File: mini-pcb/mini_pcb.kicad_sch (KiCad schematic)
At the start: 34 parts, among them J1 IN, J2 OUT, J3 Barrel_Jack_Switch, J4 AUDIO_IN_TRS, J5 AUDIO_OUT_TRS, U1 LM1117DT-5.0, U2 OPA1664D, U3 OPA1655DBV

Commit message: mini-pcb layout
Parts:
- removed J1: IN, symbol Connector:Jack-DC
- removed J2: OUT, symbol Connector:Jack-DC
- C10, C2, C3, C5, C6, C9: footprint (none) -> Capacitor_SMD:C_0805_2012Metric
- C7, C8: value 100NF -> 0.1uf
- J3: footprint GuitarPedal125B:Generic_PowerJack -> Connector_BarrelJack:BarrelJack_Horizontal
- J4, J5: footprint NMJ6HCD2:NEUTRIK_NMJ6HCD2 -> Connector_Audio:Jack_6.35mm_Neutrik_NMJ6HCD3_Horizontal
- R1, R10, R11, R12, R13, R14, R2, R3, R4, R5, R6, R7, R8, R9: footprint (none) -> Resistor_SMD:R_0603_1608Metric
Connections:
- net AUDIO_IN_JACK_LEFT_BUF: now also U2.6 (-), U2.7; no longer U2.1, U2.2 (-)
- net AUDIO_IN_JACK_RIGHT_BUF: now also U2.1, U2.2 (-); no longer U2.6 (-), U2.7
- net GND: no longer C10.2, C2.1, C6.1, C9.2, J4.R, J4.RN, J4.SN, J4.T, J4.TN, J5.R, J5.RN, J5.SN, J5.T, J5.TN, R14.2, R2.2, R8.2, R9.2
- net at C6.2, R1.1: now also U2.5 (+); no longer U2.3 (+)
- net at C2.2, R10.1: now also U2.3 (+); no longer U2.5 (+)
- new net AUDIO_IN_JACK_LEFT: C6.1, J4.T, R2.2
- new net AUDIO_IN_JACK_RIGHT: C2.1, J4.R, R9.2
- new net AUDIO_OUT_JACK_LEFT: C9.2, J5.T, R8.2
- new net AUDIO_OUT_JACK_RIGHT: C10.2, J5.R, R14.2

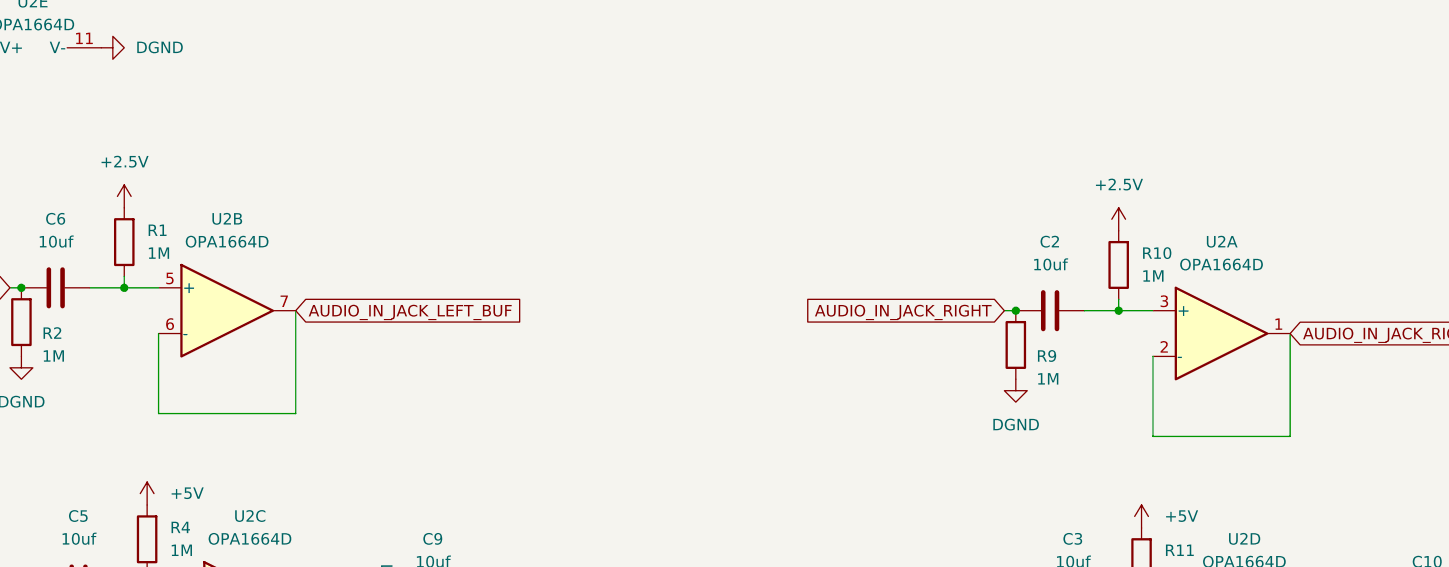
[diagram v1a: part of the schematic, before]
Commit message: eletronic simulation made
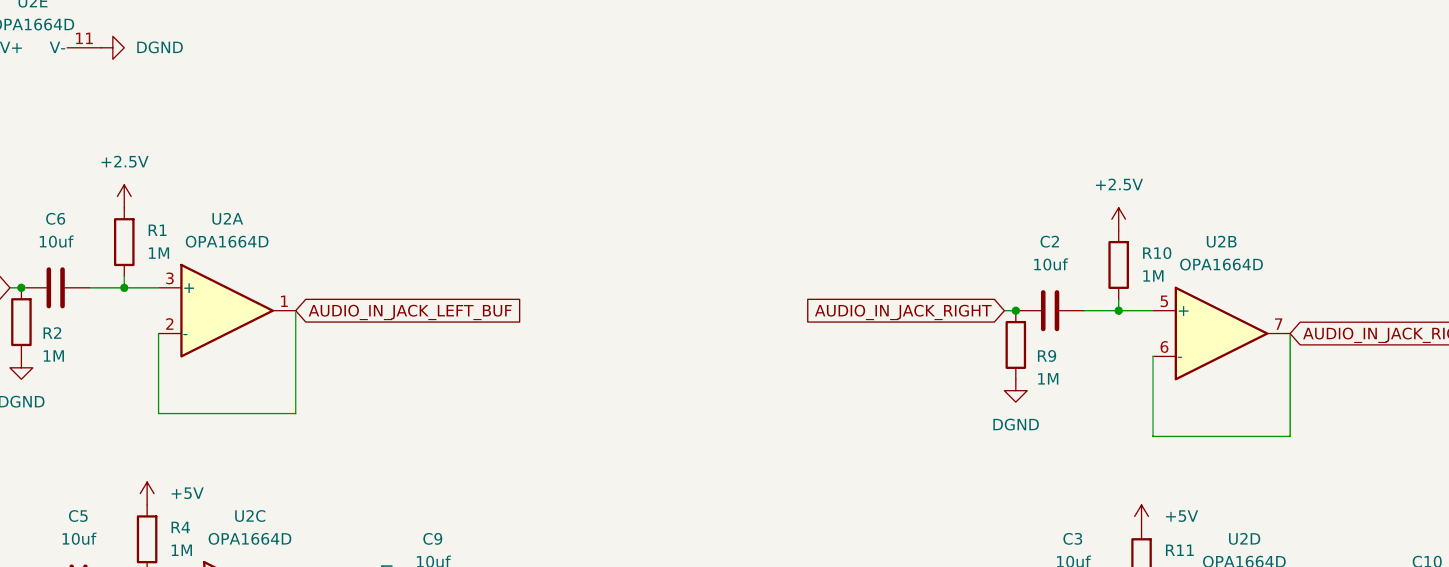
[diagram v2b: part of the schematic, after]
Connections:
- net AUDIO_IN_JACK_LEFT_BUF: now also U2.1, U2.2 (-); no longer U2.6 (-), U2.7
- net AUDIO_IN_JACK_RIGHT_BUF: now also U2.6 (-), U2.7; no longer U2.1, U2.2 (-)
- net at C6.2, R1.1: now also U2.3 (+); no longer U2.5 (+)
- net at C2.2, R10.1: now also U2.5 (+); no longer U2.3 (+)
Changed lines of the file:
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@@
-	)
-	(symbol
-		(lib_id "Amplifier_Operational:OPA1664D")
-		(at 227.33 127 0)
-		(unit 2)
-		(exclude_from_sim no)
-		(in_bom yes)
-		(on_board yes)
-		(dnp no)
-		(fields_autoplaced yes)
-		(property "Reference" "U2"
-			(at 227.33 116.84 0)
-			(effects
-				(font
-					(size 1.27 1.27)
-				)
-			)
-		)
-		(property "Value" "OPA1664D"
-			(at 227.33 119.38 0)
-			(effects
-				(font
-					(size 1.27 1.27)
-				)
-			)
-		)
-		(property "Footprint" "Package_SO:SOIC-14_3.9x8.7mm_P1.27mm"
-			(at 226.06 124.46 0)
-			(effects
-				(font
-					(size 1.27 1.27)
-				)
-				(hide yes)
-			)
-		)
-		(property "Datasheet" "https://www.ti.com/lit/ds/symlink/opa1664.pdf"
-			(at 228.6 121.92 0)
-			(effects
-				(font
-					(size 1.27 1.27)
-				)
-				(hide yes)
-			)
-		)
-		(property "Description" "Quad Low-Power, Low-Noise, Low-Distortion, Bipolar-Input SoundPlus Audio Operational Amplifiers, SOIC-14"
-			(at 227.33 127 0)
-			(effects
-				(font
-					(size 1.27 1.27)
-				)
-				(hide yes)
-			)
-		)
-		(pin "5"
-		)
-		(pin "12"
-		)
-		(pin "7"
-		)
-		(pin "8"
-		)
-		(pin "6"
-		)
-		(pin "1"
-		)
-		(pin "2"
-		)
-		(pin "10"
-		)
-		(pin "13"
-		)
-		(pin "11"
-		)
-		(pin "4"
-		)
-		(pin "14"
-		)
-		(pin "9"
-		)
-		(pin "3"
-		)
-		(instances
-			(project "mini_pcb"
-				(path "/ac8ee366-0662-41f8-9745-078ec3fbb21b"
-					(reference "U2")
-					(unit 2)
-				)
-			)
-		)
 	)
 	(symbol
@@
 	)
 	(symbol
+		(lib_id "Amplifier_Operational:OPA1664D")
+		(at 337.82 129.54 0)
+		(unit 2)
+		(exclude_from_sim no)
+		(in_bom yes)
+		(on_board yes)
+		(dnp no)
+		(fields_autoplaced yes)
+		(property "Reference" "U2"
+			(at 337.82 119.38 0)
+			(effects
+				(font
+					(size 1.27 1.27)
+				)
+			)
+		)
+		(property "Value" "OPA1664D"
+			(at 337.82 121.92 0)
+			(effects
+				(font
+					(size 1.27 1.27)
+				)
+			)
+		)
+		(property "Footprint" "Package_SO:SOIC-14_3.9x8.7mm_P1.27mm"
+			(at 336.55 127 0)
+			(effects
+				(font
+					(size 1.27 1.27)
+				)
+				(hide yes)
+			)
+		)
+		(property "Datasheet" "https://www.ti.com/lit/ds/symlink/opa1664.pdf"
+			(at 339.09 124.46 0)
+			(effects
+				(font
+					(size 1.27 1.27)
+				)
+				(hide yes)
+			)
+		)
+		(property "Description" "Quad Low-Power, Low-Noise, Low-Distortion, Bipolar-Input SoundPlus Audio Operational Amplifiers, SOIC-14"
+			(at 337.82 129.54 0)
+			(effects
+				(font
+					(size 1.27 1.27)
+				)
+				(hide yes)
+			)
+		)
+		(pin "5"
+		)
+		(pin "12"
+		)
+		(pin "7"
+		)
+		(pin "8"
+		)
+		(pin "6"
+		)
+		(pin "1"
+		)
+		(pin "2"
+		)
+		(pin "10"
+		)
+		(pin "13"
+		)
+		(pin "11"
+		)
+		(pin "4"
+		)
+		(pin "14"
+		)
+		(pin "9"
+		)
+		(pin "3"
+		)
+		(instances
+			(project "mini_pcb"
+				(path "/ac8ee366-0662-41f8-9745-078ec3fbb21b"
+					(reference "U2")
+					(unit 2)
+				)
+			)
+		)
+	)
+	(symbol
 		(lib_id "Device:C")
 		(at 318.77 127 90)
@@
 	)
 	(symbol
-		(lib_id "Amplifier_Operational:OPA1664D")
-		(at 337.82 129.54 0)
-		(unit 1)
-		(exclude_from_sim no)
-		(in_bom yes)
-		(on_board yes)
-		(dnp no)
-		(fields_autoplaced yes)
-		(property "Reference" "U2"
-			(at 337.82 119.38 0)
-			(effects
-				(font
-					(size 1.27 1.27)
-				)
-			)
-		)
-		(property "Value" "OPA1664D"
-			(at 337.82 121.92 0)
-			(effects
-				(font
-					(size 1.27 1.27)
-				)
-			)
-		)
-		(property "Footprint" "Package_SO:SOIC-14_3.9x8.7mm_P1.27mm"
-			(at 336.55 127 0)
-			(effects
-				(font
-					(size 1.27 1.27)
-				)
-				(hide yes)
-			)
-		)
-		(property "Datasheet" "https://www.ti.com/lit/ds/symlink/opa1664.pdf"
-			(at 339.09 124.46 0)
-			(effects
-				(font
-					(size 1.27 1.27)
-				)
-				(hide yes)
-			)
-		)
-		(property "Description" "Quad Low-Power, Low-Noise, Low-Distortion, Bipolar-Input SoundPlus Audio Operational Amplifiers, SOIC-14"
-			(at 337.82 129.54 0)
-			(effects
-				(font
-					(size 1.27 1.27)
-				)
-				(hide yes)
-			)
-		)
-		(pin "5"
-		)
-		(pin "12"
-		)
-		(pin "7"
-		)
-		(pin "8"
-		)
-		(pin "6"
-		)
-		(pin "1"
-		)
-		(pin "2"
-		)
-		(pin "10"
-		)
-		(pin "13"
-		)
-		(pin "11"
-		)
-		(pin "4"
-		)
-		(pin "14"
-		)
-		(pin "9"
-		)
-		(pin "3"
-		)
-		(instances
-			(project "mini_pcb"
-				(path "/ac8ee366-0662-41f8-9745-078ec3fbb21b"
-					(reference "U2")
-					(unit 1)
-				)
-			)
-		)
-	)
-	(symbol
 		(lib_id "power:+3.3V")
 		(at 135.89 171.45 0)
@@
 					(unit 1)
 				)
+			)
+		)
+	)
+	(symbol
+		(lib_id "Amplifier_Operational:OPA1664D")
+		(at 227.33 127 0)
+		(unit 1)
+		(exclude_from_sim no)
+		(in_bom yes)
+		(on_board yes)
+		(dnp no)
+		(fields_autoplaced yes)
+		(property "Reference" "U2"
+			(at 227.33 116.84 0)
+			(effects
+				(font
+					(size 1.27 1.27)
+				)
+			)
+		)
+		(property "Value" "OPA1664D"
+			(at 227.33 119.38 0)
+			(effects
+				(font
+					(size 1.27 1.27)
+				)
+			)
+		)
+		(property "Footprint" "Package_SO:SOIC-14_3.9x8.7mm_P1.27mm"
+			(at 226.06 124.46 0)
+			(effects
+				(font
+					(size 1.27 1.27)
+				)
+				(hide yes)
+			)
+		)
+		(property "Datasheet" "https://www.ti.com/lit/ds/symlink/opa1664.pdf"
+			(at 228.6 121.92 0)
+			(effects
+				(font
+					(size 1.27 1.27)
+				)
+				(hide yes)
+			)
+		)
+		(property "Description" "Quad Low-Power, Low-Noise, Low-Distortion, Bipolar-Input SoundPlus Audio Operational Amplifiers, SOIC-14"
+			(at 227.33 127 0)
+			(effects
+				(font
+					(size 1.27 1.27)
+				)
+				(hide yes)
+			)
+		)
+		(pin "5"
+		)
+		(pin "12"
+		)
+		(pin "7"
+		)
+		(pin "8"
+		)
+		(pin "6"
+		)
+		(pin "1"
+		)
+		(pin "2"
+		)
+		(pin "10"
+		)
+		(pin "13"
+		)
+		(pin "11"
+		)
+		(pin "4"
+		)
+		(pin "14"
+		)
+		(pin "9"
+		)
+		(pin "3"
+		)
+		(instances
+			(project "mini_pcb"
+				(path "/ac8ee366-0662-41f8-9745-078ec3fbb21b"
+					(reference "U2")
+					(unit 1)
+				)

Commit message: pcb update
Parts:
- removed C1, C4: 10UF, Capacitor_SMD:C_0805_2012Metric, symbol Device:C
- removed C10, C2, C3, C5, C6, C9: 10uf, Capacitor_SMD:C_0805_2012Metric, symbol Device:C
- removed C7, C8: 0.1uf, Capacitor_SMD:C_0805_2012Metric, symbol Device:C
- removed D1: 1N5817, Diode_SMD:D_SOD-123, symbol Diode:1N5817
- removed J3: Barrel_Jack_Switch, Connector_BarrelJack:BarrelJack_Horizontal, symbol Connector:Barrel_Jack_Switch
- removed R1, R10, R11, R12, R13, R14, R2, R3, R4, R5, R6, R7, R8, R9: 1M, Resistor_SMD:R_0603_1608Metric, symbol Device:R
- removed U1: LM1117DT-5.0, Package_TO_SOT_SMD:TO-252-3_TabPin2, symbol Regulator_Linear:LM1117DT-5.0
- removed U2: OPA1664D, Package_SO:SOIC-14_3.9x8.7mm_P1.27mm, symbol Amplifier_Operational:OPA1664D
- removed U3: OPA1655DBV, Package_TO_SOT_SMD:SOT-23-5, symbol Amplifier_Operational:OPA1655DBV
- added J1: Screw_Terminal_01x02, TerminalBlock:TerminalBlock_Xinya_XY308-2.54-2P_1x02_P2.54mm_Horizontal, symbol Connector:Screw_Terminal_01x02
- added U4: ESP32-C3-WROOM-02, RF_Module:ESP32-C3-WROOM-02, symbol RF_Module:ESP32-C3-WROOM-02
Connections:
- net GND is gone; now on net GNDA: J4.S, J5.S
- net +3.3VD: now also J1.1 (Pin_1)
- net at A1.28 (ADC_6): now also J1.2 (Pin_2)
- new net: U4.19 (GND), U4.9 (GND)
- no-connect marks 1 -> 0
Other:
- added sheet Input (Input.kicad_sch)
- added sheet Output (Output.kicad_sch)
- added sheet Power (power.kicad_sch)

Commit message: almost done with mini pcb
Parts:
- removed U4: ESP32-C3-WROOM-02, RF_Module:ESP32-C3-WROOM-02, symbol RF_Module:ESP32-C3-WROOM-02
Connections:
- net GNDA is gone; now on net GND: A1.20 (AGND), J4.S, J5.S
- net DGND renamed GND
- no-connect marks 0 -> 36

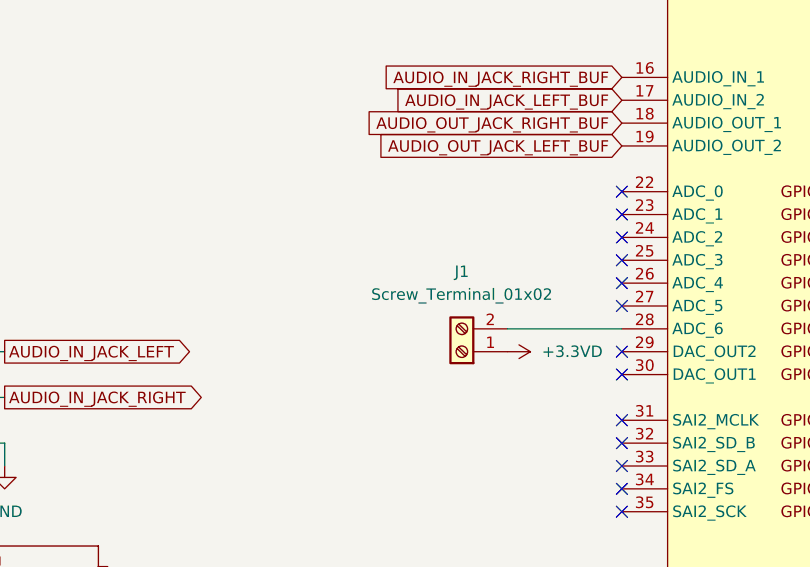
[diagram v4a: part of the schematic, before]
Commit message: made final touches and bom still needs through testing
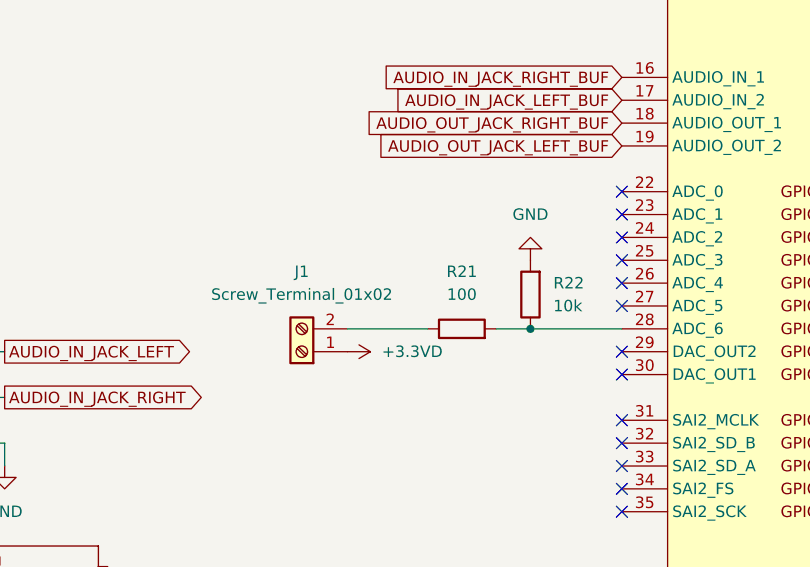
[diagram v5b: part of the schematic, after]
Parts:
- added R21: 100, Resistor_SMD:R_0603_1608Metric, symbol Device:R
- added R22: 10k, Resistor_SMD:R_0603_1608Metric, symbol Device:R
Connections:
- net GND: now also R22.2
- net at A1.28 (ADC_6): now also R21.2, R22.1; no longer J1.2 (Pin_2)
- new net: J1.2 (Pin_2), R21.1
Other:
- moved on the sheet: J1

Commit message: ordered pcb
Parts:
- added 5V1, 9V1, AUDIO_IN1, AUDIO_RAW1, GND1, GND2: TestPoint, TestPoint:TestPoint_Pad_D2.0mm, symbol Connector:TestPoint
- A1: MPN (none) -> C50984
- J1: MPN (none) -> C8465
- R21: MPN (none) -> C22775
- R22: MPN (none) -> C25804
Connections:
- net +9V: now also 9V1.1
- net AUDIO_IN_JACK_LEFT: now also AUDIO_RAW1.1
- net AUDIO_IN_JACK_RIGHT_BUF: now also AUDIO_IN1.1
- net GND: now also GND1.1, GND2.1
- new net +5V: 5V1.1

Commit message: made mini-pcb report
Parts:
- added C100: 10uf, Capacitor_SMD:C_0805_2012Metric, symbol Device:C
- added J2: 2.5V LDO, symbol Device:Battery_Cell
- added R100: 100, Resistor_SMD:R_0603_1608Metric, symbol Device:R
- added R101: 1M, Resistor_SMD:R_0603_1608Metric, symbol Device:R
- added U3: OP AMP, Package_SO:SOIC-14_3.9x8.7mm_P1.27mm, symbol Amplifier_Operational:OPA1664D
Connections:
- net GND: now also J2.2 (-)
- new net: C100.1, R100.1
- new net: C100.2, R101.1, U3.3 (+)
- new net: J2.1 (+), R101.2
- new net: U3.1, U3.2 (-)
- new net AUDIO_IN: R100.2
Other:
- note added: "0V"
- note added: "2.5V"
- note added: "3V"

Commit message: I will be re writing the code to use the daisy-embassy library because the Daisy one i have been using has a strange but crush effect when there is just a normal passthrough but the daisy-embassy example works well with my PCB also there was a testing problem earlyer with the PCB and the PCB works fine with no changes
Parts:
- removed C100: 10uf, Capacitor_SMD:C_0805_2012Metric, symbol Device:C
- removed J2: 2.5V LDO, symbol Device:Battery_Cell
- removed R100: 100, Resistor_SMD:R_0603_1608Metric, symbol Device:R
- removed R101: 1M, Resistor_SMD:R_0603_1608Metric, symbol Device:R
- removed U3: OP AMP, Package_SO:SOIC-14_3.9x8.7mm_P1.27mm, symbol Amplifier_Operational:OPA1664D
- added J6: Screw_Terminal_01x02, TerminalBlock:TerminalBlock_Xinya_XY308-2.54-2P_1x02_P2.54mm_Horizontal, symbol Connector:Screw_Terminal_01x02
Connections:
- net at A1.12 (I2C1_SCL): now also J6.1 (Pin_1)
- net at A1.13 (I2C1_SDA): now also J6.2 (Pin_2)
- no-connect marks 36 -> 34
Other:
- note removed: "0V"
- note removed: "2.5V"
- note removed: "3V"
